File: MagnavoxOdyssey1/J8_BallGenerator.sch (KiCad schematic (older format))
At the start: 19 parts

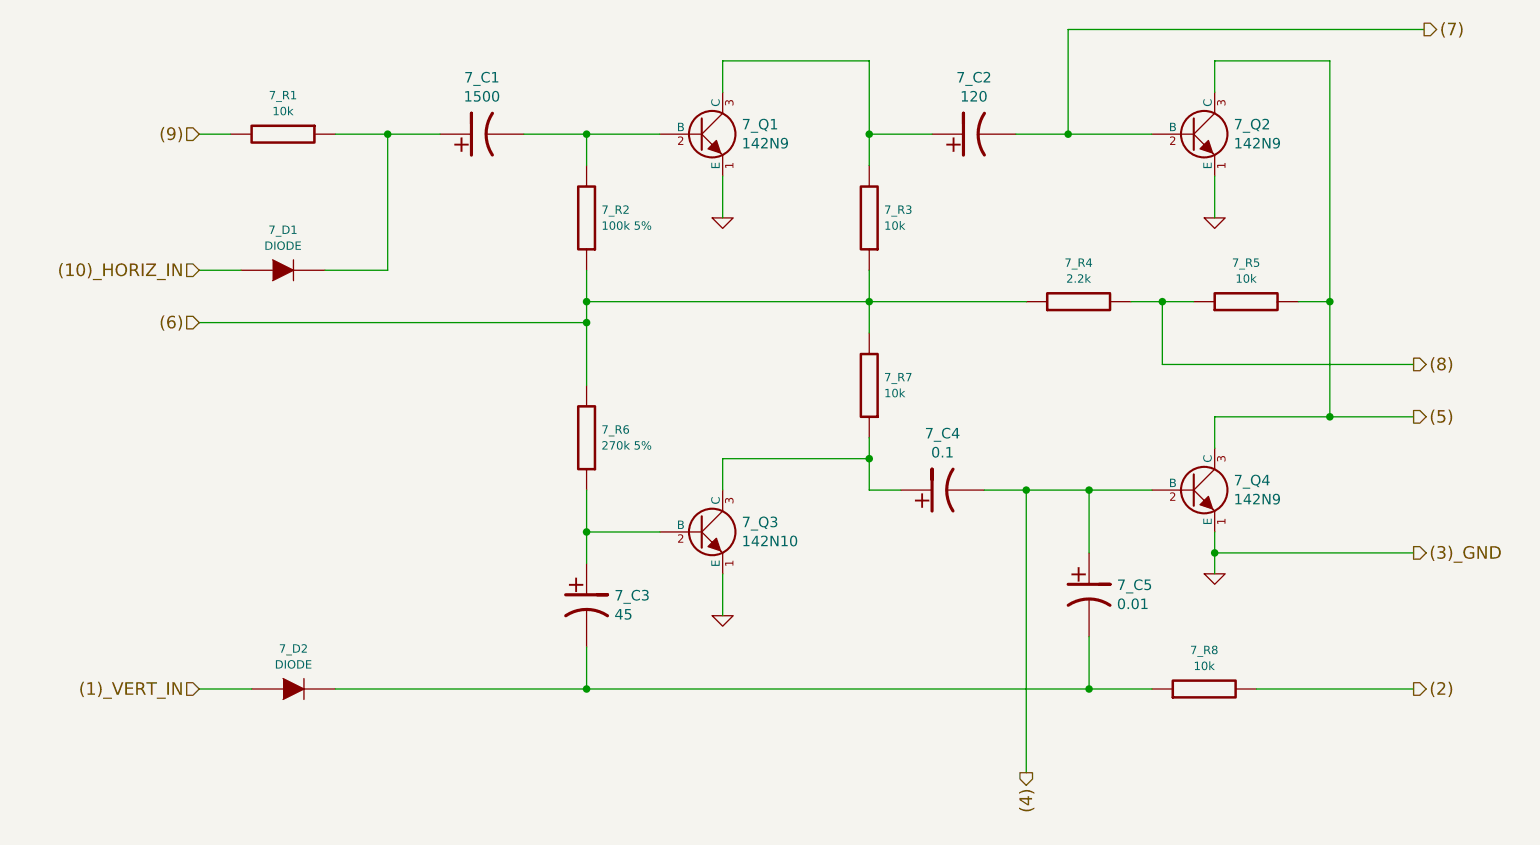
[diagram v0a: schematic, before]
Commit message: terminei de transcrever a PCB toda. Deixei de fora de propósito o estágio de modulação RF do sinal. É pouca coisa, posso adicionar amanhã ou depois... Gerei também um PDFão
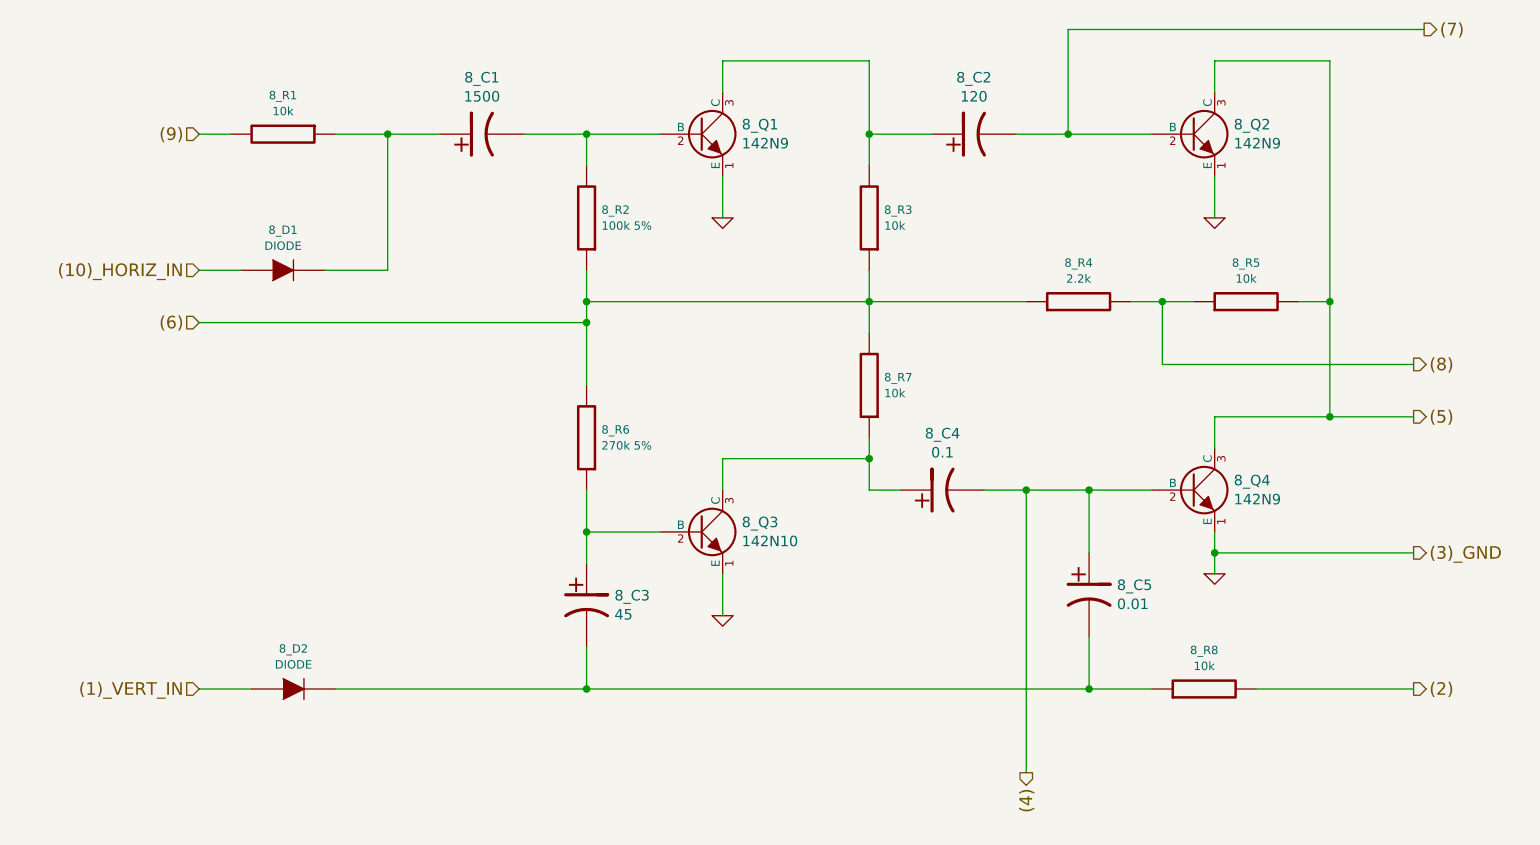
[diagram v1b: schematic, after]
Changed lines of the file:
@@
 $Descr A4 11693 8268
 encoding utf-8
-Sheet 4 8
+Sheet 8 12
 Title ""
 Date ""
@@
 AR Path="/58904212/588DCAB3" Ref="8_D1"  Part="1"
 AR Path="/588DC7EC/588DCAB3" Ref="7_D1"  Part="1"
-F 0 "7_D1" H 3500 3342 40  0000 C CNN
+F 0 "8_D1" H 3500 3342 40  0000 C CNN
 F 1 "DIODE" H 3500 3266 40  0000 C CNN
 F 2 "" H 3500 3150 60  0000 C CNN
@@
 AR Path="/58904212/588DCB1F" Ref="8_R1"  Part="1"
 AR Path="/588DC7EC/588DCB1F" Ref="7_R1"  Part="1"
-F 0 "7_R1" V 3315 2500 40  0000 C CNN
+F 0 "8_R1" V 3315 2500 40  0000 C CNN
 F 1 "10k" V 3391 2500 40  0000 C CNN
 F 2 "" V 3430 2500 30  0000 C CNN
@@
 AR Path="/58904212/588DCB74" Ref="8_C1"  Part="1"
 AR Path="/588DC7EC/588DCB74" Ref="7_C1"  Part="1"
-F 0 "7_C1" V 4720 2500 50  0000 C CNN
+F 0 "8_C1" V 4720 2500 50  0000 C CNN
 F 1 "1500" V 4629 2500 50  0000 C CNN
 F 2 "" H 4450 2500 60  0000 C CNN
@@
 AR Path="/58904212/588DCBFC" Ref="8_R2"  Part="1"
 AR Path="/588DC7EC/588DCBFC" Ref="7_R2"  Part="1"
-F 0 "7_R2" H 4879 2862 40  0000 R CNN
+F 0 "8_R2" H 4879 2862 40  0000 R CNN
 F 1 "100k 5%" H 4879 2938 40  0000 R CNN
 F 2 "" V 4880 2900 30  0000 C CNN
@@
 AR Path="/58904212/588DCC63" Ref="8_Q1"  Part="1"
 AR Path="/588DC7EC/588DCC63" Ref="7_Q1"  Part="1"
-F 0 "7_Q1" H 5691 2546 50  0000 L CNN
+F 0 "8_Q1" H 5691 2546 50  0000 L CNN
 F 1 "142N9" H 5691 2455 50  0000 L CNN
 F 2 "" H 5500 2500 60  0000 C CNN
@@
 $EndComp
 $Comp
-L GND #PWR043
+L GND #PWR069
 U 1 1 588DCD18
 P 5600 2900
-AR Path="/58904212/588DCD18" Ref="#PWR043"  Part="1"
+AR Path="/58904212/588DCD18" Ref="#PWR069"  Part="1"
 AR Path="/588DC7EC/588DCD18" Ref="#PWR027"  Part="1"
-F 0 "#PWR043" H 5600 2900 30  0001 C CNN
+F 0 "#PWR069" H 5600 2900 30  0001 C CNN
 F 1 "GND" H 5600 2830 30  0001 C CNN
 F 2 "" H 5600 2900 60  0001 C CNN
@@
 AR Path="/58904212/588DCD72" Ref="8_R3"  Part="1"
 AR Path="/588DC7EC/588DCD72" Ref="7_R3"  Part="1"
-F 0 "7_R3" H 6229 2862 40  0000 R CNN
+F 0 "8_R3" H 6229 2862 40  0000 R CNN
 F 1 "10k" H 6229 2938 40  0000 R CNN
 F 2 "" V 6230 2900 30  0000 C CNN
@@
 AR Path="/58904212/588DCDCD" Ref="8_C2"  Part="1"
 AR Path="/588DC7EC/588DCDCD" Ref="7_C2"  Part="1"
-F 0 "7_C2" V 7070 2500 50  0000 C CNN
+F 0 "8_C2" V 7070 2500 50  0000 C CNN
 F 1 "120" V 6979 2500 50  0000 C CNN
 F 2 "" H 6800 2500 60  0000 C CNN
@@
 AR Path="/58904212/588DCE86" Ref="8_Q2"  Part="1"
 AR Path="/588DC7EC/588DCE86" Ref="7_Q2"  Part="1"
-F 0 "7_Q2" H 8041 2546 50  0000 L CNN
+F 0 "8_Q2" H 8041 2546 50  0000 L CNN
 F 1 "142N9" H 8041 2455 50  0000 L CNN
 F 2 "" H 7850 2500 60  0000 C CNN
@@
 $EndComp
 $Comp
-L GND #PWR044
+L GND #PWR070
 U 1 1 588DCE8C
 P 7950 2900
-AR Path="/58904212/588DCE8C" Ref="#PWR044"  Part="1"
+AR Path="/58904212/588DCE8C" Ref="#PWR070"  Part="1"
 AR Path="/588DC7EC/588DCE8C" Ref="#PWR028"  Part="1"
-F 0 "#PWR044" H 7950 2900 30  0001 C CNN
+F 0 "#PWR070" H 7950 2900 30  0001 C CNN
 F 1 "GND" H 7950 2830 30  0001 C CNN
 F 2 "" H 7950 2900 60  0001 C CNN
@@
 AR Path="/58904212/588DD03A" Ref="8_R6"  Part="1"
 AR Path="/588DC7EC/588DD03A" Ref="7_R6"  Part="1"
-F 0 "7_R6" H 4879 3912 40  0000 R CNN
+F 0 "8_R6" H 4879 3912 40  0000 R CNN
 F 1 "270k 5%" H 4879 3988 40  0000 R CNN
 F 2 "" V 4880 3950 30  0000 C CNN
@@
 AR Path="/58904212/588DD5E2" Ref="8_Q3"  Part="1"
 AR Path="/588DC7EC/588DD5E2" Ref="7_Q3"  Part="1"
-F 0 "7_Q3" H 5691 4446 50  0000 L CNN
+F 0 "8_Q3" H 5691 4446 50  0000 L CNN
 F 1 "142N10" H 5691 4355 50  0000 L CNN
 F 2 "" H 5500 4400 60  0000 C CNN
@@
 $EndComp
 $Comp
-L GND #PWR045
+L GND #PWR071
 U 1 1 588DD5E8
 P 5600 4800
-AR Path="/58904212/588DD5E8" Ref="#PWR045"  Part="1"
+AR Path="/58904212/588DD5E8" Ref="#PWR071"  Part="1"
 AR Path="/588DC7EC/588DD5E8" Ref="#PWR029"  Part="1"
-F 0 "#PWR045" H 5600 4800 30  0001 C CNN
+F 0 "#PWR071" H 5600 4800 30  0001 C CNN
 F 1 "GND" H 5600 4730 30  0001 C CNN
 F 2 "" H 5600 4800 60  0001 C CNN
@@
 AR Path="/58904212/588DD6AF" Ref="8_R7"  Part="1"
 AR Path="/588DC7EC/588DD6AF" Ref="7_R7"  Part="1"
-F 0 "7_R7" H 6229 3662 40  0000 R CNN
+F 0 "8_R7" H 6229 3662 40  0000 R CNN
 F 1 "10k" H 6229 3738 40  0000 R CNN
 F 2 "" V 6230 3700 30  0000 C CNN
@@
 AR Path="/58904212/588DD883" Ref="8_C4"  Part="1"
 AR Path="/588DC7EC/588DD883" Ref="7_C4"  Part="1"
-F 0 "7_C4" V 6920 4200 50  0000 C CNN
+F 0 "8_C4" V 6920 4200 50  0000 C CNN
 F 1 "0.1" V 6829 4200 50  0000 C CNN
 F 2 "" H 6650 4200 60  0000 C CNN
@@
 AR Path="/58904212/588DD8E3" Ref="8_C5"  Part="1"
 AR Path="/588DC7EC/588DD8E3" Ref="7_C5"  Part="1"
-F 0 "7_C5" H 7483 4746 50  0000 L CNN
+F 0 "8_C5" H 7483 4746 50  0000 L CNN
 F 1 "0.01" H 7483 4655 50  0000 L CNN
 F 2 "" H 7350 4700 60  0000 C CNN
@@
 AR Path="/58904212/588DDB1C" Ref="8_C3"  Part="1"
 AR Path="/588DC7EC/588DDB1C" Ref="7_C3"  Part="1"
-F 0 "7_C3" H 5083 4796 50  0000 L CNN
+F 0 "8_C3" H 5083 4796 50  0000 L CNN
 F 1 "45" H 5083 4705 50  0000 L CNN
 F 2 "" H 4950 4750 60  0000 C CNN
@@
 AR Path="/58904212/588DDD4B" Ref="8_R8"  Part="1"
 AR Path="/588DC7EC/588DDD4B" Ref="7_R8"  Part="1"
-F 0 "7_R8" V 8085 5150 40  0000 C CNN
+F 0 "8_R8" V 8085 5150 40  0000 C CNN
 F 1 "10k" V 8009 5150 40  0000 C CNN
 F 2 "" V 7830 5150 30  0000 C CNN
@@
 AR Path="/58904212/588DDF3A" Ref="8_Q4"  Part="1"
 AR Path="/588DC7EC/588DDF3A" Ref="7_Q4"  Part="1"
-F 0 "7_Q4" H 8041 4246 50  0000 L CNN
+F 0 "8_Q4" H 8041 4246 50  0000 L CNN
 F 1 "142N9" H 8041 4155 50  0000 L CNN
 F 2 "" H 7850 4200 60  0000 C CNN
@@
 $EndComp
 $Comp
-L GND #PWR046
+L GND #PWR072
 U 1 1 588DDF40
 P 7950 4600
-AR Path="/58904212/588DDF40" Ref="#PWR046"  Part="1"
+AR Path="/58904212/588DDF40" Ref="#PWR072"  Part="1"
 AR Path="/588DC7EC/588DDF40" Ref="#PWR030"  Part="1"
-F 0 "#PWR046" H 7950 4600 30  0001 C CNN
+F 0 "#PWR072" H 7950 4600 30  0001 C CNN
 F 1 "GND" H 7950 4530 30  0001 C CNN
 F 2 "" H 7950 4600 60  0001 C CNN
@@
 AR Path="/58904212/588DE2ED" Ref="8_R4"  Part="1"
 AR Path="/588DC7EC/588DE2ED" Ref="7_R4"  Part="1"
-F 0 "7_R4" V 7485 3300 40  0000 C CNN
+F 0 "8_R4" V 7485 3300 40  0000 C CNN
 F 1 "2.2k" V 7409 3300 40  0000 C CNN
 F 2 "" V 7230 3300 30  0000 C CNN
@@
 AR Path="/58904212/588DE379" Ref="8_R5"  Part="1"
 AR Path="/588DC7EC/588DE379" Ref="7_R5"  Part="1"
-F 0 "7_R5" V 8285 3300 40  0000 C CNN
+F 0 "8_R5" V 8285 3300 40  0000 C CNN
 F 1 "10k" V 8209 3300 40  0000 C CNN
 F 2 "" V 8030 3300 30  0000 C CNN
@@
 AR Path="/58904212/588DE8DA" Ref="8_D2"  Part="1"
 AR Path="/588DC7EC/588DE8DA" Ref="7_D2"  Part="1"
-F 0 "7_D2" H 3550 5342 40  0000 C CNN
+F 0 "8_D2" H 3550 5342 40  0000 C CNN
 F 1 "DIODE" H 3550 5266 40  0000 C CNN
 F 2 "" H 3550 5150 60  0000 C CNN
